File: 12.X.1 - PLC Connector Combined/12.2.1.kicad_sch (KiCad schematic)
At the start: 32 parts, among them J301 Conn_01x01_PAD, J302 Conn_01x01_PAD, J303 Conn_01x01_PAD, J304 Conn_01x01_PAD, J305 Conn_01x01_PAD, J306 Conn_01x01_PAD, J307 Conn_01x01_PAD, J308 Conn_01x01_PAD, J309 Conn_01x01_PAD, J310 Conn_01x01_PAD, J311 Conn_01x01_PAD, J312 Conn_01x01_PAD, J313 Conn_01x01_PAD, J314 Conn_01x01_PAD, J315 Conn_01x01_PAD, J316 Conn_01x01_PAD, J317 DB128L-5.08-3P-BK-S, J318 DB128L-5.08-2P-BK-S, J319 DB128L-5.08-2P-BK-S, J320 DB128L-5.08-2P-BK-S, J321 B04B-XASK-1

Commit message: worked on layout, added V-Cut lines
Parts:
- J301, J302, J303, J304, J305, J306, J307, J308, J309, J310, J311, J312, J313, J314, J315, J316: footprint PCB_FOOTPRINT_Library:Conn_pin_PLC -> PCB_Library:Conn_pin_PLC
- J317: footprint PCB_FOOTPRINT_Library:XY128V-A-5.08-3P -> PCB_Library:XY128V-A-5.08-3P
- J318, J319, J320: footprint PCB_FOOTPRINT_Library:1729128 -> PCB_Library:1729128
- J321: footprint PCB_FOOTPRINT_Library:CONN_B04B-XASK-1_JST -> PCB_Library:CONN_B04B-XASK-1_JST
- JP301, JP302, JP303: footprint PCB_FOOTPRINT_Library:SolderJumper-2_P2.6mm_Open_RoundedPad2.0x3mm -> PCB_Library:SolderJumper-2_P2.6mm_Open_RoundedPad2.0x3mm
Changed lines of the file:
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@@
       (effects (font (size 1.27 1.27)))
     )
-    (property "Footprint" "PCB_FOOTPRINT_Library:Conn_pin_PLC" (at 50.8 27.94 0)
+    (property "Footprint" "PCB_Library:Conn_pin_PLC" (at 50.8 27.94 0)
       (effects (font (size 1.27 1.27)) hide)
     )
@@
       (effects (font (size 1.27 1.27)))
     )
-    (property "Footprint" "PCB_FOOTPRINT_Library:Conn_pin_PLC" (at 88.9 35.56 0)
+    (property "Footprint" "PCB_Library:Conn_pin_PLC" (at 88.9 35.56 0)
       (effects (font (size 1.27 1.27)) hide)
     )
@@
       (effects (font (size 1.27 1.27)))
     )
-    (property "Footprint" "PCB_FOOTPRINT_Library:Conn_pin_PLC" (at 88.9 27.94 0)
+    (property "Footprint" "PCB_Library:Conn_pin_PLC" (at 88.9 27.94 0)
       (effects (font (size 1.27 1.27)) hide)
     )
@@
       (effects (font (size 1.27 1.27)))
     )
-    (property "Footprint" "PCB_FOOTPRINT_Library:SolderJumper-2_P2.6mm_Open_RoundedPad2.0x3mm" (at 38.1 52.07 0)
+    (property "Footprint" "PCB_Library:SolderJumper-2_P2.6mm_Open_RoundedPad2.0x3mm" (at 38.1 52.07 0)
       (effects (font (size 1.27 1.27)) hide)
     )
@@
       (effects (font (size 1.27 1.27)))
     )
-    (property "Footprint" "PCB_FOOTPRINT_Library:Conn_pin_PLC" (at 130.81 104.14 0)
+    (property "Footprint" "PCB_Library:Conn_pin_PLC" (at 130.81 104.14 0)
       (effects (font (size 1.27 1.27)) hide)
     )
@@
       (effects (font (size 1.27 1.27)))
     )
-    (property "Footprint" "PCB_FOOTPRINT_Library:Conn_pin_PLC" (at 49.53 172.72 0)
+    (property "Footprint" "PCB_Library:Conn_pin_PLC" (at 49.53 172.72 0)
       (effects (font (size 1.27 1.27)) hide)
     )
@@
       (effects (font (size 1.27 1.27)) (justify left))
     )
-    (property "Footprint" "PCB_FOOTPRINT_Library:1729128" (at 233.68 233.35 0)
+    (property "Footprint" "PCB_Library:1729128" (at 233.68 233.35 0)
       (effects (font (size 1.27 1.27)) (justify left top) hide)
     )
@@
       (effects (font (size 1.27 1.27)))
     )
-    (property "Footprint" "PCB_FOOTPRINT_Library:Conn_pin_PLC" (at 130.81 115.57 0)
+    (property "Footprint" "PCB_Library:Conn_pin_PLC" (at 130.81 115.57 0)
       (effects (font (size 1.27 1.27)) hide)
     )
@@
       (effects (font (size 1.524 1.524)) (justify left))
     )
-    (property "Footprint" "PCB_FOOTPRINT_Library:CONN_B04B-XASK-1_JST" (at 259.08 99.06 0)
+    (property "Footprint" "PCB_Library:CONN_B04B-XASK-1_JST" (at 259.08 99.06 0)
       (effects (font (size 1.27 1.27) italic) hide)
     )
@@
       (effects (font (size 1.27 1.27)))
     )
-    (property "Footprint" "PCB_FOOTPRINT_Library:Conn_pin_PLC" (at 92.71 115.57 0)
+    (property "Footprint" "PCB_Library:Conn_pin_PLC" (at 92.71 115.57 0)
       (effects (font (size 1.27 1.27)) hide)
     )
@@
       (effects (font (size 1.27 1.27)))
     )
-    (property "Footprint" "PCB_FOOTPRINT_Library:SolderJumper-2_P2.6mm_Open_RoundedPad2.0x3mm" (at 40.64 144.78 0)
+    (property "Footprint" "PCB_Library:SolderJumper-2_P2.6mm_Open_RoundedPad2.0x3mm" (at 40.64 144.78 0)
       (effects (font (size 1.27 1.27)) hide)
     )
@@
       (effects (font (size 1.27 1.27)))
     )
-    (property "Footprint" "PCB_FOOTPRINT_Library:Conn_pin_PLC" (at 87.63 162.56 0)
+    (property "Footprint" "PCB_Library:Conn_pin_PLC" (at 87.63 162.56 0)
       (effects (font (size 1.27 1.27)) hide)
     )
@@
       (effects (font (size 1.27 1.27)) (justify left))
     )
-    (property "Footprint" "PCB_FOOTPRINT_Library:1729128" (at 236.22 199.06 0)
+    (property "Footprint" "PCB_Library:1729128" (at 236.22 199.06 0)
       (effects (font (size 1.27 1.27)) (justify left top) hide)
     )
@@
       (effects (font (size 1.27 1.27)))
     )
-    (property "Footprint" "PCB_FOOTPRINT_Library:Conn_pin_PLC" (at 49.53 162.56 0)
+    (property "Footprint" "PCB_Library:Conn_pin_PLC" (at 49.53 162.56 0)
       (effects (font (size 1.27 1.27)) hide)
     )
@@
       (effects (font (size 1.27 1.27)))
     )
-    (property "Footprint" "PCB_FOOTPRINT_Library:SolderJumper-2_P2.6mm_Open_RoundedPad2.0x3mm" (at 38.1 90.17 0)
+    (property "Footprint" "PCB_Library:SolderJumper-2_P2.6mm_Open_RoundedPad2.0x3mm" (at 38.1 90.17 0)
       (effects (font (size 1.27 1.27)) hide)
     )
@@
       (effects (font (size 1.27 1.27)))
     )
-    (property "Footprint" "PCB_FOOTPRINT_Library:Conn_pin_PLC" (at 54.61 77.47 0)
+    (property "Footprint" "PCB_Library:Conn_pin_PLC" (at 54.61 77.47 0)
       (effects (font (size 1.27 1.27)) hide)
     )
@@
       (effects (font (size 1.27 1.27)))
     )
-    (property "Footprint" "PCB_FOOTPRINT_Library:Conn_pin_PLC" (at 87.63 172.72 0)
+    (property "Footprint" "PCB_Library:Conn_pin_PLC" (at 87.63 172.72 0)
       (effects (font (size 1.27 1.27)) hide)
     )
@@
       (effects (font (size 1.27 1.27)) (justify left))
     )
-    (property "Footprint" "PCB_FOOTPRINT_Library:1729128" (at 233.68 163.5 0)
+    (property "Footprint" "PCB_Library:1729128" (at 233.68 163.5 0)
       (effects (font (size 1.27 1.27)) (justify left top) hide)
     )
@@
       (effects (font (size 1.27 1.27)))
     )
-    (property "Footprint" "PCB_FOOTPRINT_Library:Conn_pin_PLC" (at 92.71 104.14 0)
+    (property "Footprint" "PCB_Library:Conn_pin_PLC" (at 92.71 104.14 0)
       (effects (font (size 1.27 1.27)) hide)
     )
@@
       (effects (font (size 1.27 1.27)))
     )
-    (property "Footprint" "PCB_FOOTPRINT_Library:Conn_pin_PLC" (at 92.71 68.58 0)
+    (property "Footprint" "PCB_Library:Conn_pin_PLC" (at 92.71 68.58 0)
       (effects (font (size 1.27 1.27)) hide)
     )
@@
       (effects (font (size 1.27 1.27)))
     )
-    (property "Footprint" "PCB_FOOTPRINT_Library:Conn_pin_PLC" (at 54.61 68.58 0)
+    (property "Footprint" "PCB_Library:Conn_pin_PLC" (at 54.61 68.58 0)
       (effects (font (size 1.27 1.27)) hide)
     )
@@
       (effects (font (size 1.27 1.27)))
     )
-    (property "Footprint" "PCB_FOOTPRINT_Library:Conn_pin_PLC" (at 92.71 77.47 0)
+    (property "Footprint" "PCB_Library:Conn_pin_PLC" (at 92.71 77.47 0)
       (effects (font (size 1.27 1.27)) hide)
     )
@@
       (effects (font (size 1.27 1.27)) (justify left))
     )
-    (property "Footprint" "PCB_FOOTPRINT_Library:XY128V-A-5.08-3P" (at 233.68 120.32 0)
+    (property "Footprint" "PCB_Library:XY128V-A-5.08-3P" (at 233.68 120.32 0)
       (effects (font (size 1.27 1.27)) (justify left top) hide)
     )
@@
       (effects (font (size 1.27 1.27)))
     )
-    (property "Footprint" "PCB_FOOTPRINT_Library:Conn_pin_PLC" (at 50.8 35.56 0)
-      (effects (font (size 1.27 1.27)) hide)
-    )
+    (property "Footprint" "PCB_Library:Conn_pin_PLC" (at 50.8 35.56 0)
+      (effects (font (size 1.27 1.27)) hide)
+    )

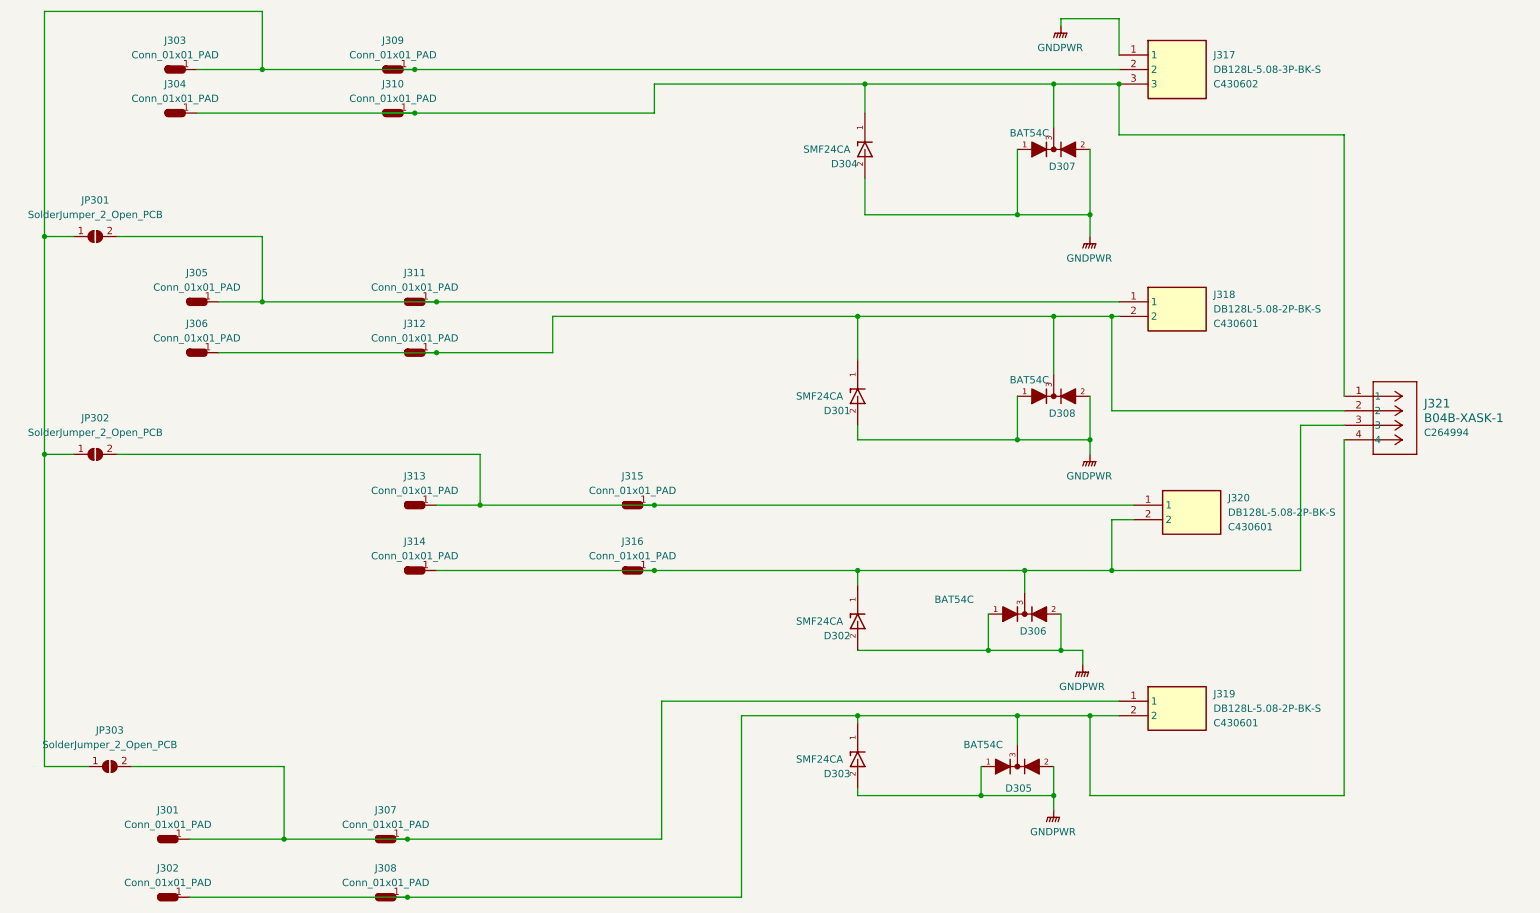
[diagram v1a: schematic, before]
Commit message: change pcb edge cuts
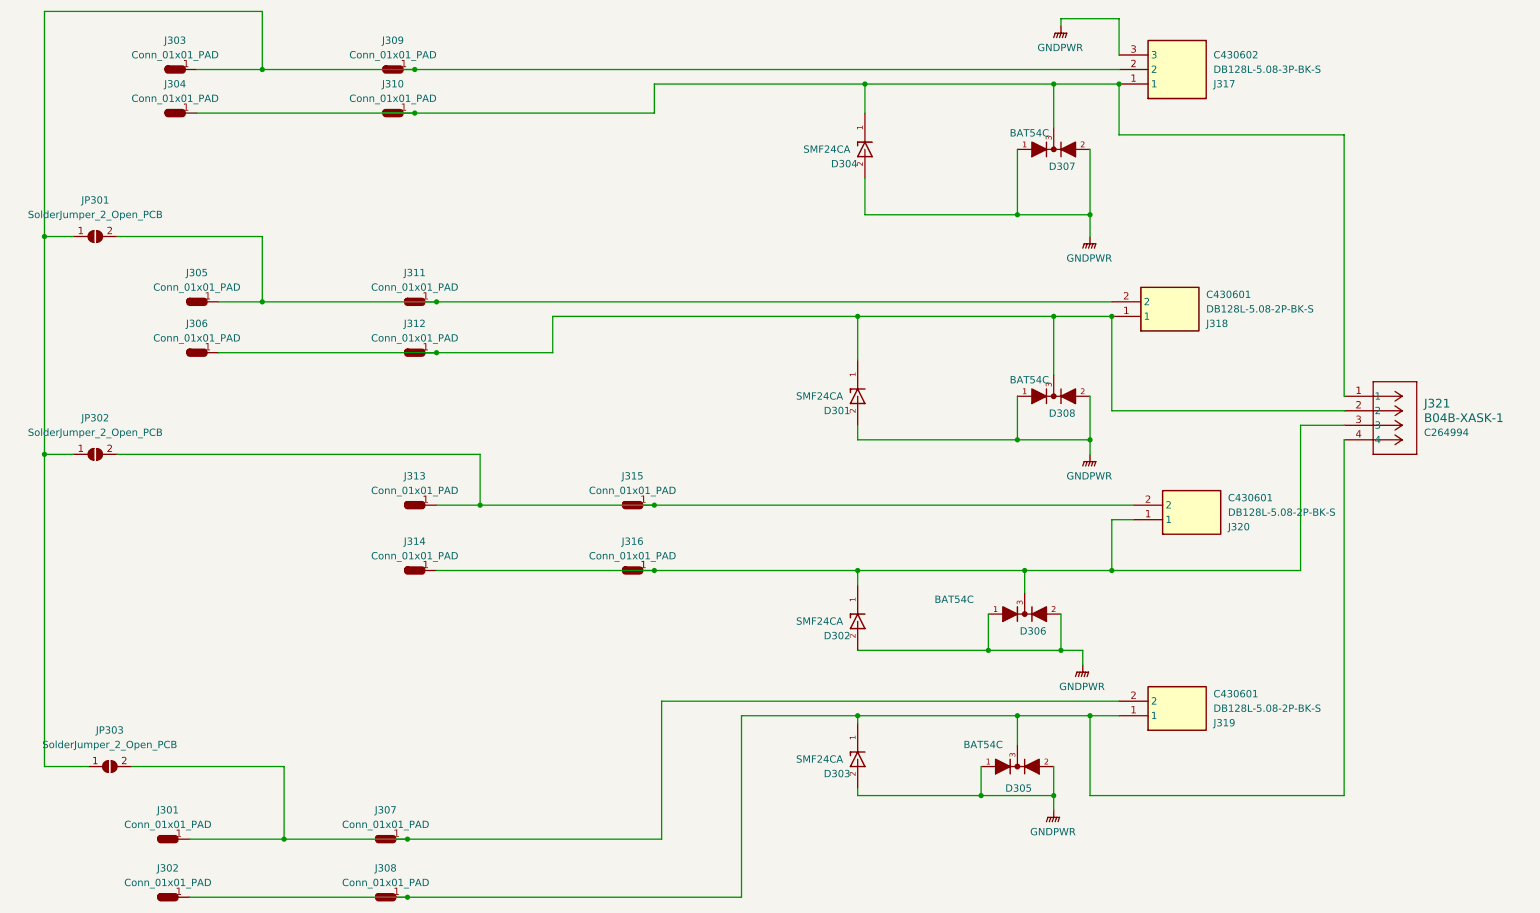
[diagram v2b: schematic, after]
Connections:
- net GNDPWR: now also J317.3; no longer J317.1
- net at D304.1, D307.3, J304.1 (Pin_1)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: now also J317.1; no longer J317.3
- net at D302.1, D306.3, J314.1 (Pin_1)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: now also J320.1; no longer J320.2
- net at J305.1 (Pin_1), J311.1 (Pin_1), JP301.2 (B): now also J318.2; no longer J318.1
- net at J313.1 (Pin_1), J315.1 (Pin_1), JP302.2 (B): now also J320.2; no longer J320.1
- net at D303.1, D305.3, J302.1 (Pin_1)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: now also J319.1; no longer J319.2
- net at J301.1 (Pin_1), J307.1 (Pin_1), JP303.2 (B): now also J319.2; no longer J319.1
- net at D301.1, D308.3, J306.1 (Pin_1)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: now also J318.1; no longer J318.2
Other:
- moved on the sheet: J318
